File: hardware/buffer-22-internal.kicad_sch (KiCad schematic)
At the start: 9 parts, among them U10 74LVC8T245, U11 74LVC8T245, U9 74LVC8T245

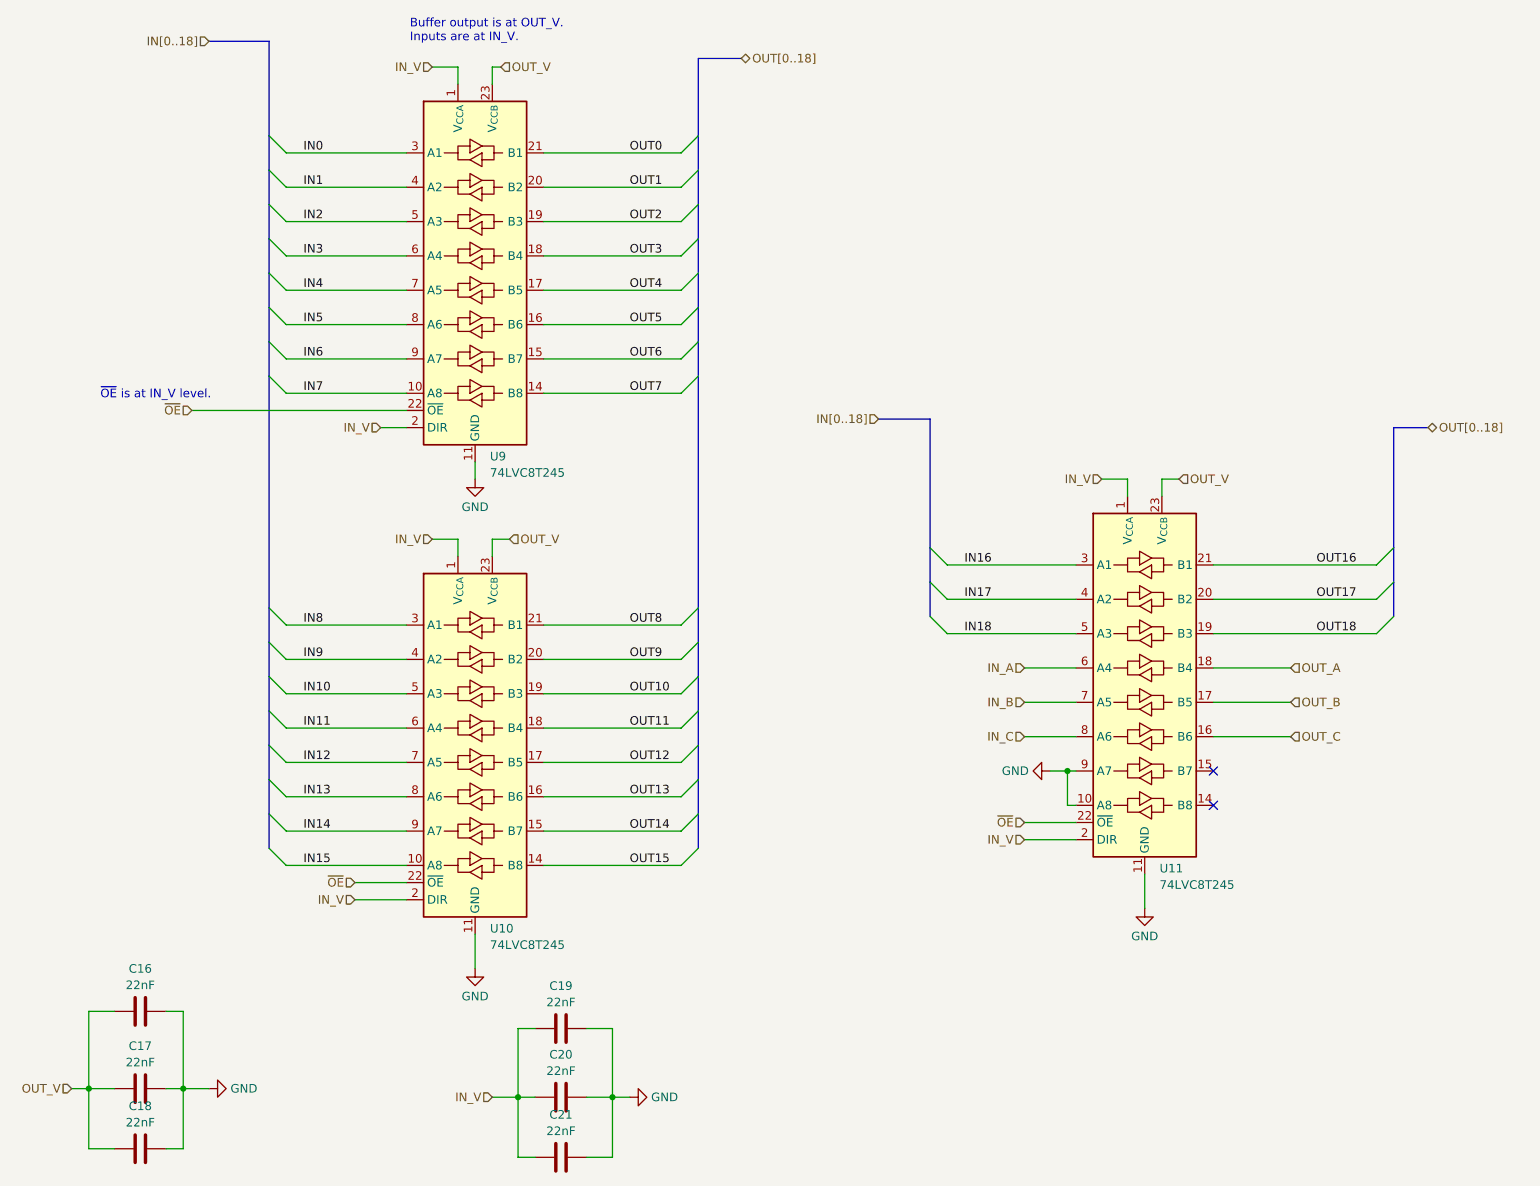
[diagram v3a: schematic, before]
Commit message: Update KiCad to 9.0
Open and save every schematic and board file without changing anything
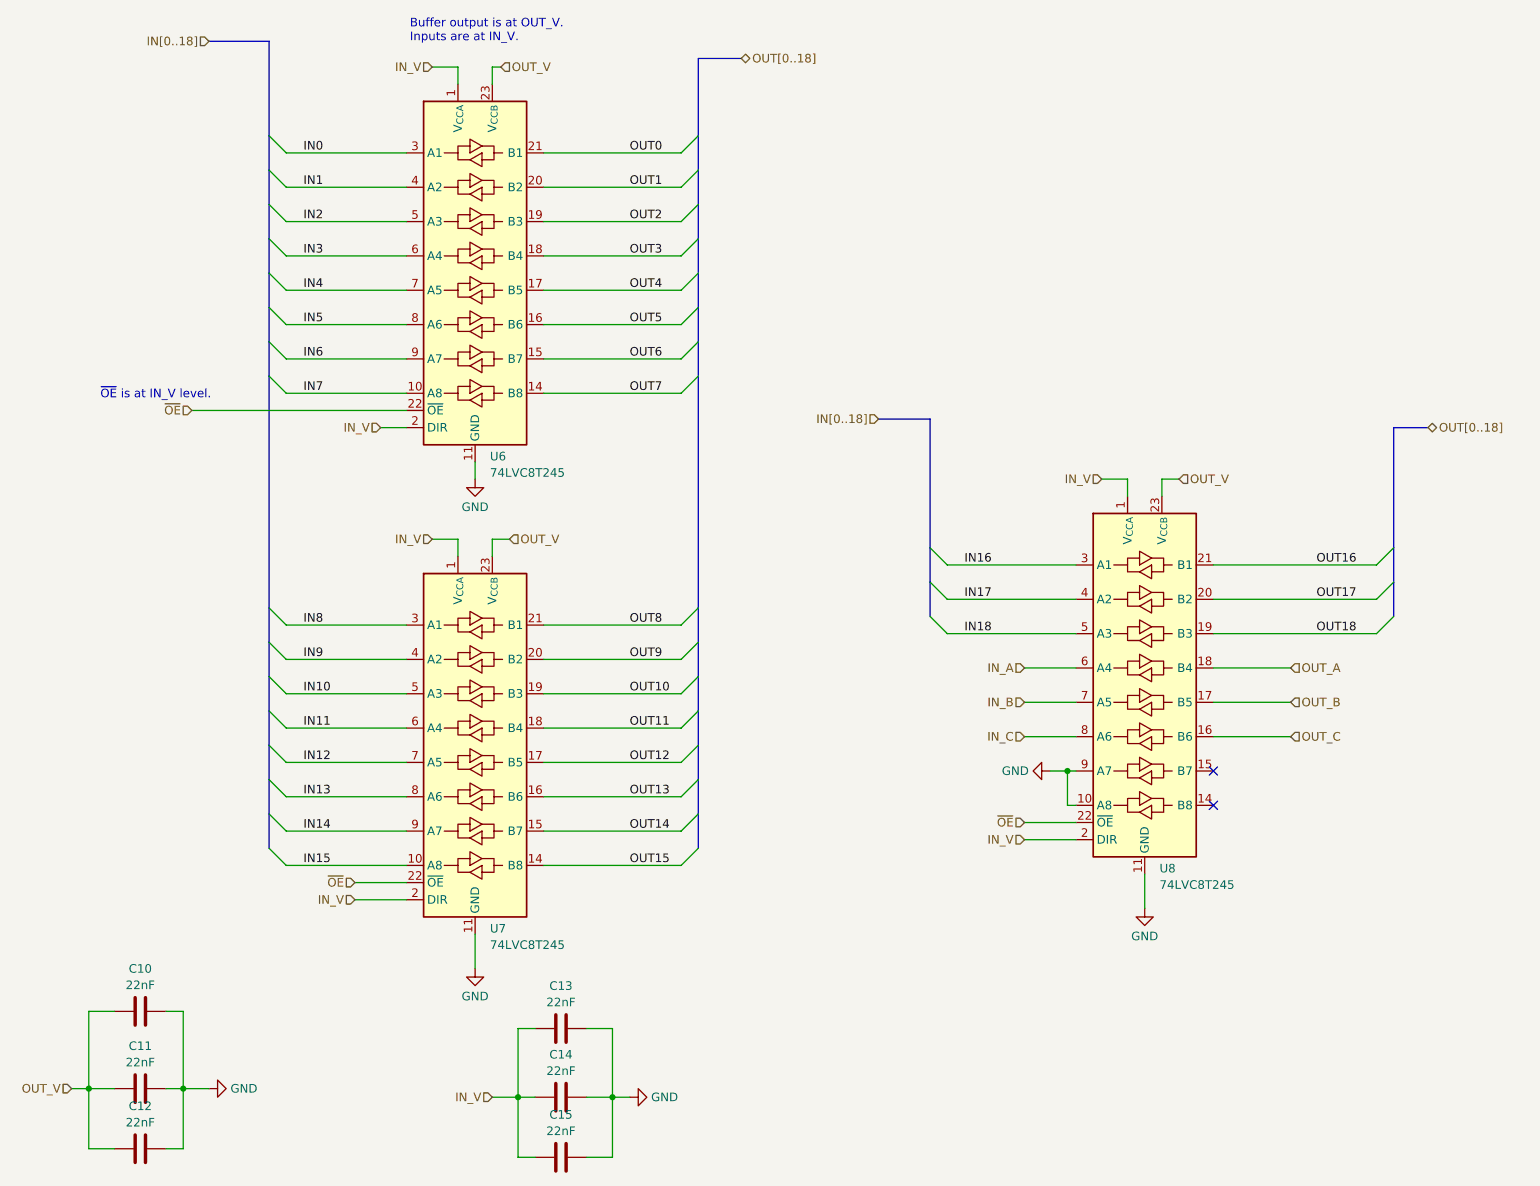
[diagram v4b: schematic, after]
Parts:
- renumbered C16 to C10, C17 to C11, C18 to C12, C19 to C13, C20 to C14, C21 to C15, U9 to U6, U10 to U7, U11 to U8

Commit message: Move SRAM bank board design into shareable subsheet
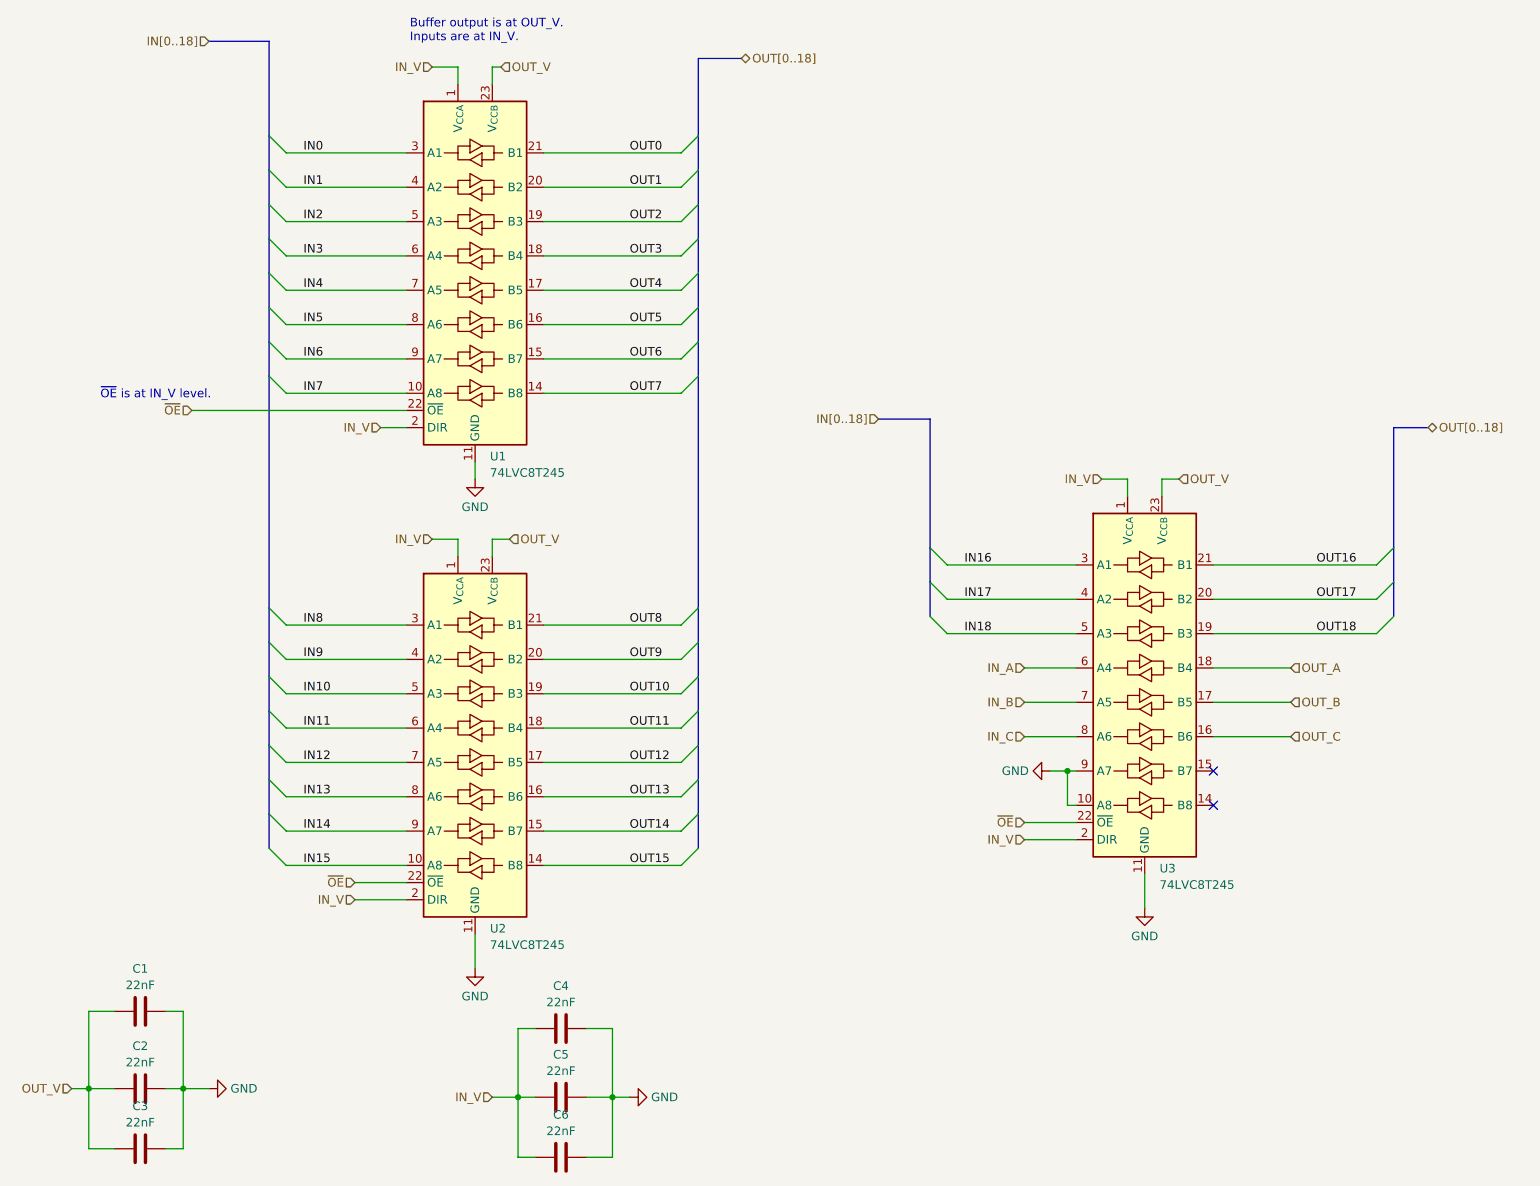
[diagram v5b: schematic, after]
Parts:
- renumbered C10 to C1, C11 to C2, C12 to C3, C13 to C4, C14 to C5, C15 to C6, U6 to U1, U7 to U2, U8 to U3

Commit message: Reannotate schematics and drop debug bridges
Parts are now numbered starting at 0 for cart, 100 for SRAM, 300 for
microcontroller.

Also, drop debug bridges that made routing more difficult and had the
same names across prototype boards.

Hopefully this will help avoid naming conflicts for the unified PCB.

Also, redo prototype PCB layouts.

Now that all the names have changed, update board layouts.
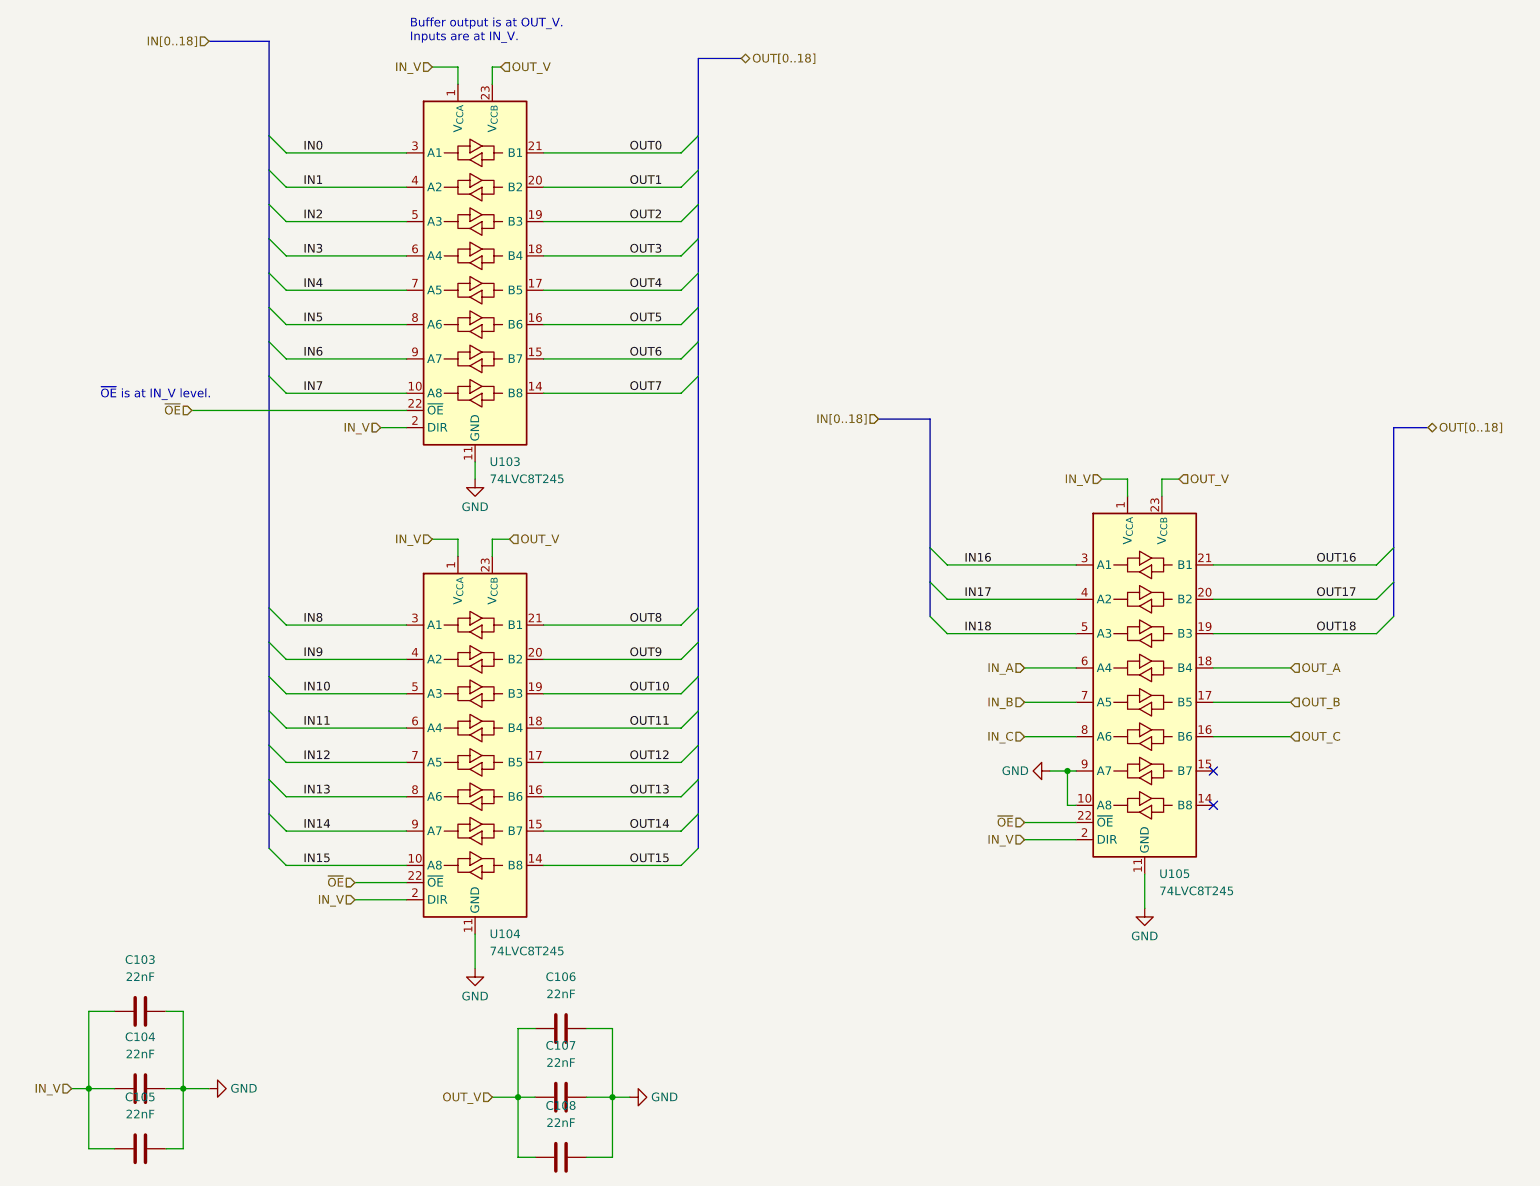
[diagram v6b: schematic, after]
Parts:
- renumbered C1 to C103, C2 to C104, C3 to C105, C4 to C106, C5 to C107, C6 to C108, U1 to U103, U2 to U104, U3 to U105
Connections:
- net IN_V: now also C103.1, C104.1, C105.1; no longer C106.1, C107.1, C108.1
- net OUT_V: now also C106.1, C107.1, C108.1; no longer C103.1, C104.1, C105.1
